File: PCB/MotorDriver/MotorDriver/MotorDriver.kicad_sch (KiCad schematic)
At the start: 1 part, among them J3 XT30PW-M

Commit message: :sparkles: 基板V2完成！！！
MotorDriverになってるけど普通にMain PCB V2ですわ！
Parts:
- removed J3: XT30PW-M, Connector_AMASS:AMASS_XT30PW-M_1x02_P2.50mm_Horizontal, symbol Connector_Generic:Conn_01x02
- added C25, C26: 22u, Capacitor_SMD:C_1206_3216Metric_Pad1.33x1.80mm_HandSolder, symbol Device:C_Small
- added C26 (x11): 0.1u, Capacitor_SMD:C_0603_1608Metric_Pad1.08x0.95mm_HandSolder, symbol Device:C_Small
- added C3: 220u, Capacitor_SMD:CP_Elec_10x10, symbol Device:C_Polarized
- added C8: 220u, Capacitor_SMD:CP_Elec_6.3x5.4, symbol Device:C_Polarized
- added D19 (x5), D4: LED, LED_SMD:LED_0603_1608Metric_Pad1.05x0.95mm_HandSolder, symbol Device:LED
- added D20: D_Schottky, Diode_SMD:D_SOD-323_HandSoldering, symbol Device:D_Schottky
- added D9: ＧＳ１０１０ＦＬ, Diode_SMD:D_SOD-123F, symbol Device:D
- added J13 (x2): JST-XH, Connector_JST:JST_XH_B2B-XH-A_1x02_P2.50mm_Vertical, symbol Connector:Conn_01x02_Pin
- added J14 (x3), J5, J6, J7: JST-XH, Connector_JST:JST_XH_B3B-XH-A_1x03_P2.50mm_Vertical, symbol Connector:Conn_01x03_Pin
- added J2, J8 (x5), J9: JST-XH, Connector_JST:JST_XH_B4B-XH-A_1x04_P2.50mm_Vertical, symbol Connector:Conn_01x04_Pin
- added J3 (x3): XT30PW-M, Connector_AMASS:AMASS_XT30PW-M_1x02_P2.50mm_Horizontal, symbol Connector_Generic:Conn_01x02
- added J5 (x6): JST-XH, Connector_PinHeader_2.54mm:PinHeader_1x03_P2.54mm_Vertical, symbol Connector:Conn_01x03_Pin
- added LS1: PKLCS1212E4001-R1, PKLCS1212E4001-R1:PKL, symbol PKLCS1212E4001-R1:PKLCS1212E4001-R1
- added Q10: NMOS, Package_TO_SOT_SMD:SOT-23, symbol Simulation_SPICE:NMOS
- added Q3: TJ60S04M3L, Package_TO_SOT_SMD:TO-252-2, symbol Simulation_SPICE:PMOS
- added R1, R2, R6, R7, R9: 1k, Resistor_SMD:R_0603_1608Metric_Pad0.98x0.95mm_HandSolder, symbol Device:R
- added R15, R16, R17, R18, R19, R20, R21, R6: 4.7k, Resistor_SMD:R_0402_1005Metric_Pad0.72x0.64mm_HandSolder, symbol Device:R
- added R3 (x2), R4, R5, R8: 10k, Resistor_SMD:R_0603_1608Metric_Pad0.98x0.95mm_HandSolder, symbol Device:R
- added SW1 (x2): SW_Push, newinov-kicad:SKRPACE010, symbol Switch:SW_Push
- added SW2: SW_DPST_x2, Button_Switch_THT:SW_E-Switch_EG1271_SPDT, symbol Switch:SW_DPST_x2
- added U1: Pico, MCU_RaspberryPi_and_Boards:RPi_Pico_SMD_TH, symbol MCU_RaspberryPi_and_Boards:Pico
- added U15: AZ1117CH-3.3TR, Package_TO_SOT_SMD:SOT-223-3_TabPin2, symbol sushi_lib:AZ1117CH-3.3TR
- added U3: TCA9548APWR, Package_SO:TSSOP-24_4.4x7.8mm_P0.65mm, symbol Interface_Expansion:TCA9548APWR
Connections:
- net +12V: now also C3.1, D9.2 (A), J14.2 (Pin_2), J14.2 (Pin_2), J14.2 (Pin_2), LS1.P, Q3.2 (D), R3.1, R8.1
- net Motor1A: now also J3.1 (Pin_1)
- net Motor1B: now also J3.2 (Pin_2)
- new net: D19.2 (A), R2.2
- new net: U3.1 (A0), U3.2 (A1), U3.21 (A2)
- new net: D4.2 (A), R8.2
- new net: D19.2 (A), R1.2
- new net: D19.2 (A), R6.2
- new net: D19.2 (A), R7.2
- new net: LS1.N, Q10.1 (D), R3.2
- new net: D19.2 (A), R9.2
- new net: Q3.1 (G), R5.2, SW2.1 (A)
- new net +3V3: C26.1, C26.1, C26.1, C26.1, C26.1, C26.1, C26.1, C26.1, C26.1, C26.1, C8.1, D20.1 (K), J13.1 (Pin_1), J2.3 (Pin_3), J5.2 (Pin_2), J5.2 (Pin_2), J5.2 (Pin_2), J5.2 (Pin_2), J5.2 (Pin_2), J5.2 (Pin_2), J5.2 (Pin_2), J6.2 (Pin_2), J7.2 (Pin_2), J8.3 (Pin_3), J8.3 (Pin_3), J8.3 (Pin_3), J8.3 (Pin_3), J8.3 (Pin_3), J9.3 (Pin_3), R15.1, R16.1, R17.1, R18.1, R19.1, R20.1, R21.1, R3.1, R4.1, R6.1, R6.1, U1.35 (ADC_VREF), U1.36 (3V3), U15.2 (OUTPUT), U3.24 (VCC), U3.3 (~{RESET})
- new net +BATT: C26.2, J3.2 (Pin_2), Q3.3 (S), R5.1
- new net 12VIN: C25.1, C26.1, D9.1 (K), U15.3 (INPUT)
- new net ADC0: J5.1 (Pin_1), U1.31 (GPIO26_ADC0)
- new net ADC1: J6.1 (Pin_1), U1.32 (GPIO27_ADC1)
- new net ADC2: J7.1 (Pin_1), U1.34 (GPIO28_ADC2)
- new net Alive_LED: R9.1, U1.22 (GPIO17)
- new net BUZZER: Q10.2 (G), U1.27 (GPIO21)
- new net Debug_LED: R7.1, U1.21 (GPIO16)
- new net EMG: J13.1 (Pin_1), U1.4 (GPIO2)
- new net GND: C25.2, C26.1, C26.2, C26.2, C26.2, C26.2, C26.2, C26.2, C26.2, C26.2, C26.2, C26.2, C26.2, C3.2, C8.2, D19.1 (K), D19.1 (K), D19.1 (K), D19.1 (K), D19.1 (K), D20.2 (A), D4.1 (K), J13.2 (Pin_2), J13.2 (Pin_2), J14.3 (Pin_3), J14.3 (Pin_3), J14.3 (Pin_3), J2.4 (Pin_4), J3.1 (Pin_1), J5.3 (Pin_3), J5.3 (Pin_3), J5.3 (Pin_3), J5.3 (Pin_3), J5.3 (Pin_3), J5.3 (Pin_3), J5.3 (Pin_3), J6.3 (Pin_3), J7.3 (Pin_3), J8.4 (Pin_4), J8.4 (Pin_4), J8.4 (Pin_4), J8.4 (Pin_4), J8.4 (Pin_4), J9.4 (Pin_4), Q10.3 (S), SW1.1, SW1.1, SW2.2 (B), U1.13 (GND), U1.18 (GND), U1.23 (GND), U1.28 (GND), U1.3 (GND), U1.33 (AGND), U1.38 (GND), U1.42 (GND), U1.8 (GND), U15.1 (GND), U3.12 (GND)
- new net GPIO10: J5.1 (Pin_1), U1.14 (GPIO10)
- new net GPIO11: J5.1 (Pin_1), U1.15 (GPIO11)
- new net GPIO12: J5.1 (Pin_1), U1.16 (GPIO12)
- new net GPIO13: J5.1 (Pin_1), U1.17 (GPIO13)
- new net GPIO14: J5.1 (Pin_1), U1.19 (GPIO14)
- new net GPIO15: J5.1 (Pin_1), U1.20 (GPIO15)
- new net INA1: R1.1, U1.10 (GPIO7)
- new net INA2: U1.9 (GPIO6)
- new net INB1: R2.1, U1.12 (GPIO9)
- new net INB2: U1.11 (GPIO8)
- new net Motor2A: J3.2 (Pin_2)
- new net Motor2B: J3.1 (Pin_1)
- new net RUN: SW1.2, U1.30 (RUN)
- new net RX0: J2.2 (Pin_2), U1.2 (GPIO1)
- new net SCL: J8.2 (Pin_2), J9.2 (Pin_2), R4.2, U1.7 (GPIO5), U3.22 (SCL)
- new net SCL0: J8.2 (Pin_2), R6.2, U3.5 (SC0)
- new net SCL1: J8.2 (Pin_2), R16.2, U3.7 (SC1)
- new net SCL2: J8.2 (Pin_2), R18.2, U3.9 (SC2)
- new net SCL3: J8.2 (Pin_2), R20.2, U3.11 (SC3)
- new net SDA: J8.1 (Pin_1), J9.1 (Pin_1), R3.2, U1.6 (GPIO4), U3.23 (SDA)
- new net SDA0: J8.1 (Pin_1), R15.2, U3.4 (SD0)
- new net SDA1: J8.1 (Pin_1), R17.2, U3.6 (SD1)
- new net SDA2: J8.1 (Pin_1), R19.2, U3.8 (SD2)
- new net SDA3: J8.1 (Pin_1), R21.2, U3.10 (SD3)
- new net SW: SW1.2, U1.5 (GPIO3)
- new net Servo1: J14.1 (Pin_1), U1.24 (GPIO18)
- new net Servo2: J14.1 (Pin_1), U1.25 (GPIO19)
- new net Servo3: J14.1 (Pin_1), U1.26 (GPIO20)
- new net TX0: J2.1 (Pin_1), U1.1 (GPIO0)
- no-connect marks 0 -> 13
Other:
- added sheet MotorDriveUnit1 (H-Bridge.kicad_sch)
- note added: "Button"
- note added: "Buzzer"
- note added: "Connector"
- note added: "EMG"
- note added: "I2C"
- note added: "I2C MUX"
- note added: "INPUT"
- note added: "LED"
- note added: "MCU"
- note added: "Motor"
- note added: "ON/OFF"
- note added: "POWER"
- note added: "Reset"
- note added: "Servo"

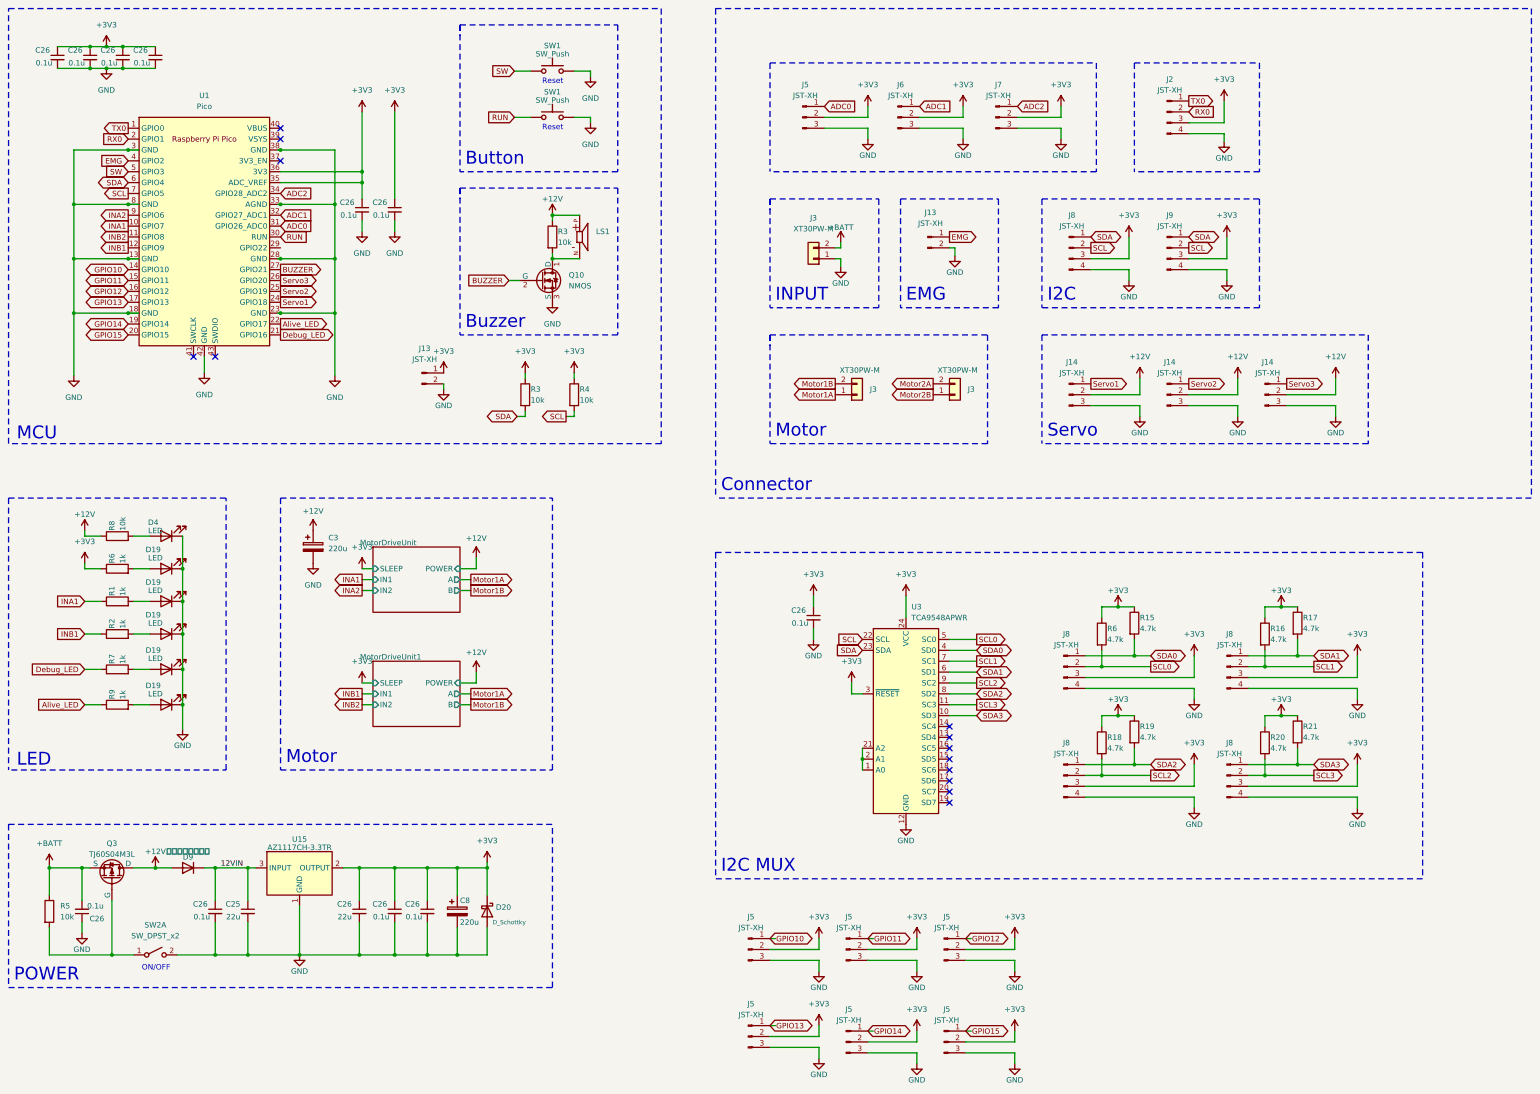
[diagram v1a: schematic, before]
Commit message: Revert ":sparkles: ビアの追加"
This reverts commit f41483c75bcc19d71434e040f06f5bb4b5903eec.
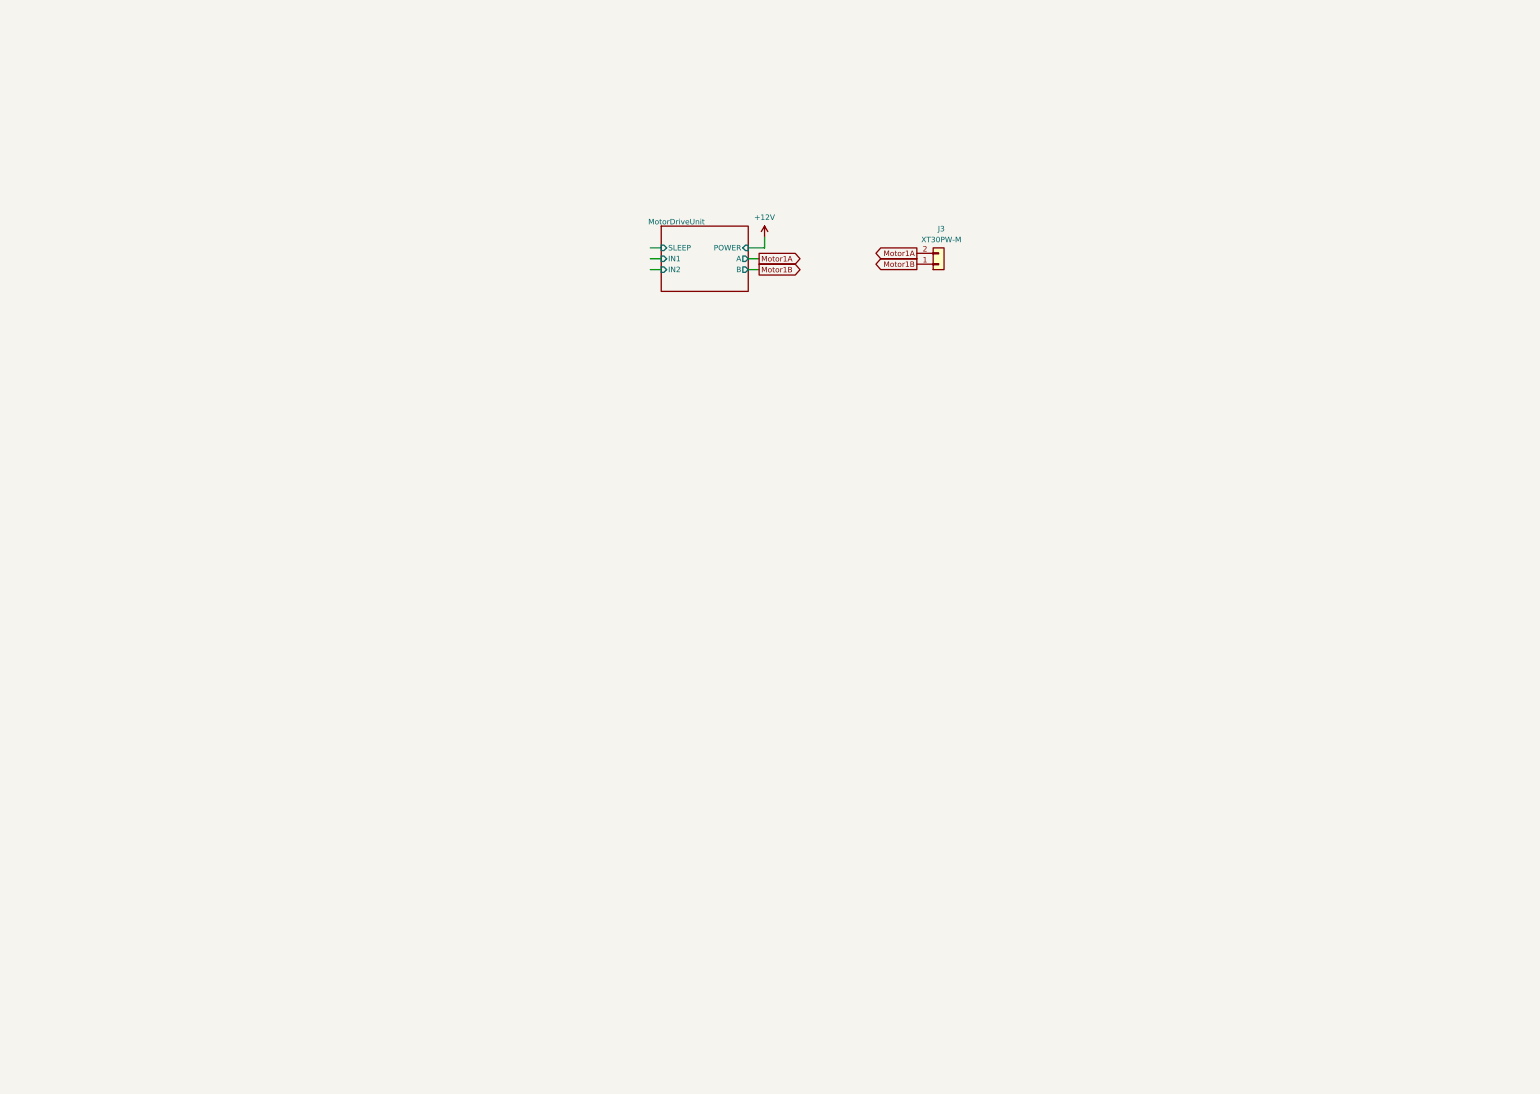
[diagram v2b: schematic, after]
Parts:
- removed C25, C26: 22u, Capacitor_SMD:C_1206_3216Metric_Pad1.33x1.80mm_HandSolder, symbol Device:C_Small
- removed C26 (x11): 0.1u, Capacitor_SMD:C_0603_1608Metric_Pad1.08x0.95mm_HandSolder, symbol Device:C_Small
- removed C3: 220u, Capacitor_SMD:CP_Elec_10x10, symbol Device:C_Polarized
- removed C8: 220u, Capacitor_SMD:CP_Elec_6.3x5.4, symbol Device:C_Polarized
- removed D19 (x5), D4: LED, LED_SMD:LED_0603_1608Metric_Pad1.05x0.95mm_HandSolder, symbol Device:LED
- removed D20: D_Schottky, Diode_SMD:D_SOD-323_HandSoldering, symbol Device:D_Schottky
- removed D9: ＧＳ１０１０ＦＬ, Diode_SMD:D_SOD-123F, symbol Device:D
- removed J13 (x2): JST-XH, Connector_JST:JST_XH_B2B-XH-A_1x02_P2.50mm_Vertical, symbol Connector:Conn_01x02_Pin
- removed J14 (x3), J5, J6, J7: JST-XH, Connector_JST:JST_XH_B3B-XH-A_1x03_P2.50mm_Vertical, symbol Connector:Conn_01x03_Pin
- removed J2, J8 (x5), J9: JST-XH, Connector_JST:JST_XH_B4B-XH-A_1x04_P2.50mm_Vertical, symbol Connector:Conn_01x04_Pin
- removed J3 (x3): XT30PW-M, Connector_AMASS:AMASS_XT30PW-M_1x02_P2.50mm_Horizontal, symbol Connector_Generic:Conn_01x02
- removed J5 (x6): JST-XH, Connector_PinHeader_2.54mm:PinHeader_1x03_P2.54mm_Vertical, symbol Connector:Conn_01x03_Pin
- removed LS1: PKLCS1212E4001-R1, PKLCS1212E4001-R1:PKL, symbol PKLCS1212E4001-R1:PKLCS1212E4001-R1
- removed Q10: NMOS, Package_TO_SOT_SMD:SOT-23, symbol Simulation_SPICE:NMOS
- removed Q3: TJ60S04M3L, Package_TO_SOT_SMD:TO-252-2, symbol Simulation_SPICE:PMOS
- removed R1, R2, R6, R7, R9: 1k, Resistor_SMD:R_0603_1608Metric_Pad0.98x0.95mm_HandSolder, symbol Device:R
- removed R15, R16, R17, R18, R19, R20, R21, R6: 4.7k, Resistor_SMD:R_0402_1005Metric_Pad0.72x0.64mm_HandSolder, symbol Device:R
- removed R3 (x2), R4, R5, R8: 10k, Resistor_SMD:R_0603_1608Metric_Pad0.98x0.95mm_HandSolder, symbol Device:R
- removed SW1 (x2): SW_Push, newinov-kicad:SKRPACE010, symbol Switch:SW_Push
- removed SW2: SW_DPST_x2, Button_Switch_THT:SW_E-Switch_EG1271_SPDT, symbol Switch:SW_DPST_x2
- removed U1: Pico, MCU_RaspberryPi_and_Boards:RPi_Pico_SMD_TH, symbol MCU_RaspberryPi_and_Boards:Pico
- removed U15: AZ1117CH-3.3TR, Package_TO_SOT_SMD:SOT-223-3_TabPin2, symbol sushi_lib:AZ1117CH-3.3TR
- removed U3: TCA9548APWR, Package_SO:TSSOP-24_4.4x7.8mm_P0.65mm, symbol Interface_Expansion:TCA9548APWR
- added J3: XT30PW-M, Connector_AMASS:AMASS_XT30PW-M_1x02_P2.50mm_Horizontal, symbol Connector_Generic:Conn_01x02
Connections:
- net Motor1A: now also J3.2 (Pin_2)
- net Motor1B: now also J3.1 (Pin_1)
- no-connect marks 13 -> 0
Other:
- removed sheet MotorDriveUnit1
- note removed: "Button"
- note removed: "Buzzer"
- note removed: "Connector"
- note removed: "EMG"
- note removed: "I2C"
- note removed: "I2C MUX"
- note removed: "INPUT"
- note removed: "LED"
- note removed: "MCU"
- note removed: "Motor"
- note removed: "ON/OFF"
- note removed: "POWER"
- note removed: "Reset"
- note removed: "Servo"
